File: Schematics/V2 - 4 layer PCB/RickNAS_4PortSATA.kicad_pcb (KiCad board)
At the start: 4 copper layers, 136.1 x 56.4 mm, 38 parts, among them J1 2227595-1, J10 10076579-002C-TRLF, J2 Conn_01x03, J3 Conn_01x03, J6 POWER, J7 10076579-002C-TRLF, J8 10076579-002C-TRLF, J9 10076579-002C-TRLF, U1 CH32V003FxPx, U2 TLV1117-33

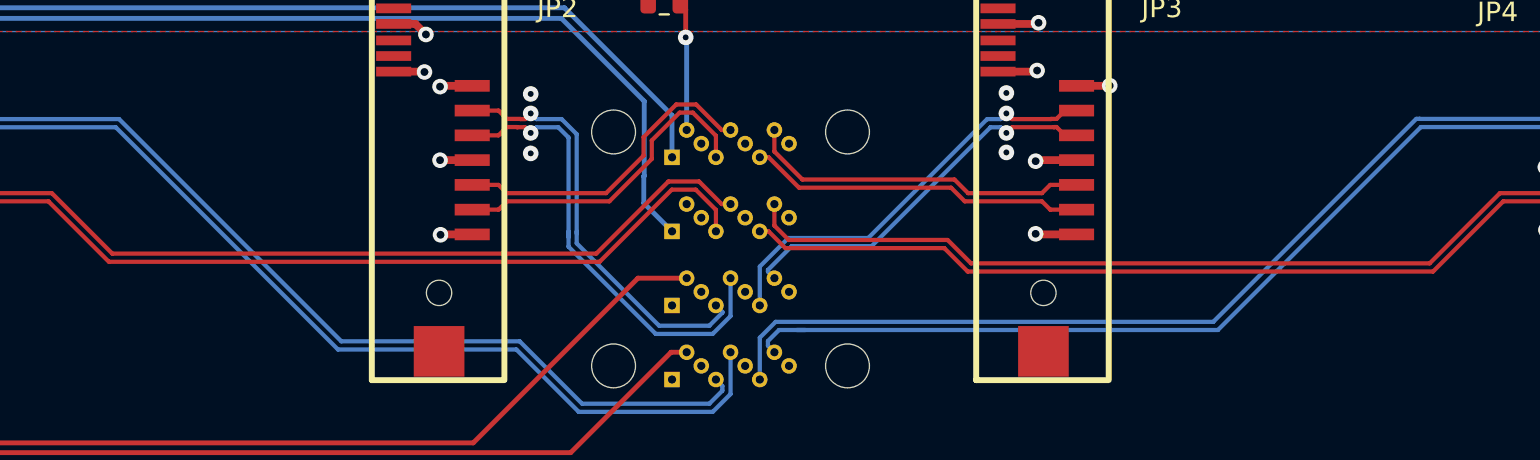
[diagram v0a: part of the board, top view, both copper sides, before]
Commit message: Tune TX pair skew with bumps on B.Cu
KiCad-measured intra-pair skew before -> after:
TX0 1.9555 -> <0.001 mm (4 bumps on TX0+)
TX1 2.1315 -> 0.0025 mm (2+2 bumps on TX1+)
TX2 1.4995 -> <0.001 mm (3 bumps on TX2-)
TX3 1.9555 -> <0.001 mm (4 bumps on TX3-)

Bumps: 45-degree chamfers (0.1 mm), height 0.36-0.38 mm (<2x pair gap),
top/spacing 0.55 mm, outward from partner. DRC unchanged (29 known),
0 unconnected, nothing new within 0.6 mm of the pairs.

Co-Authored-By: Claude Opus 5 <noreply@anthropic.com>
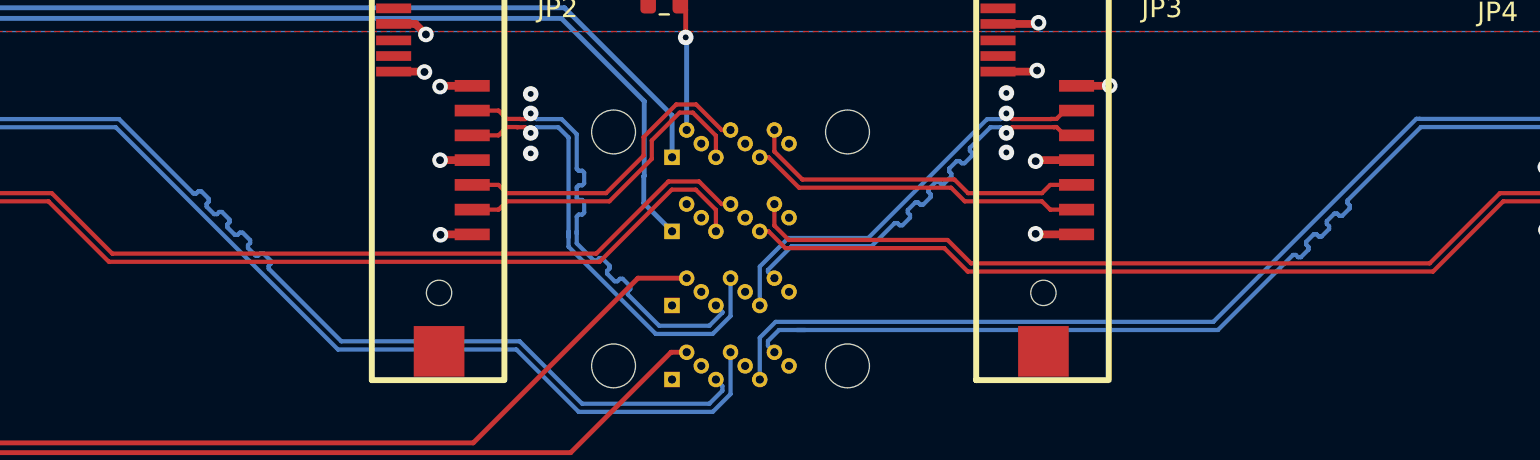
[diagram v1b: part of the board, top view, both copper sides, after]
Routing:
- net /TX1+: track 21.8 -> 24.0 mm
- net /TX3-: track 19.8 -> 21.8 mm
- net /TX0+: track 51.3 -> 53.2 mm
- net /TX2-: track 53.0 -> 54.5 mm
